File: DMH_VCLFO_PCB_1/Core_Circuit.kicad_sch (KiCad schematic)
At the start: 73 parts, among them Q1 BC548, Q2 BC558, Q3 BC548, Q4 BC548, Q5 BS170, Q6 J113, Q7 BC548, U10 TL074, U11 TL074, U12 TL074

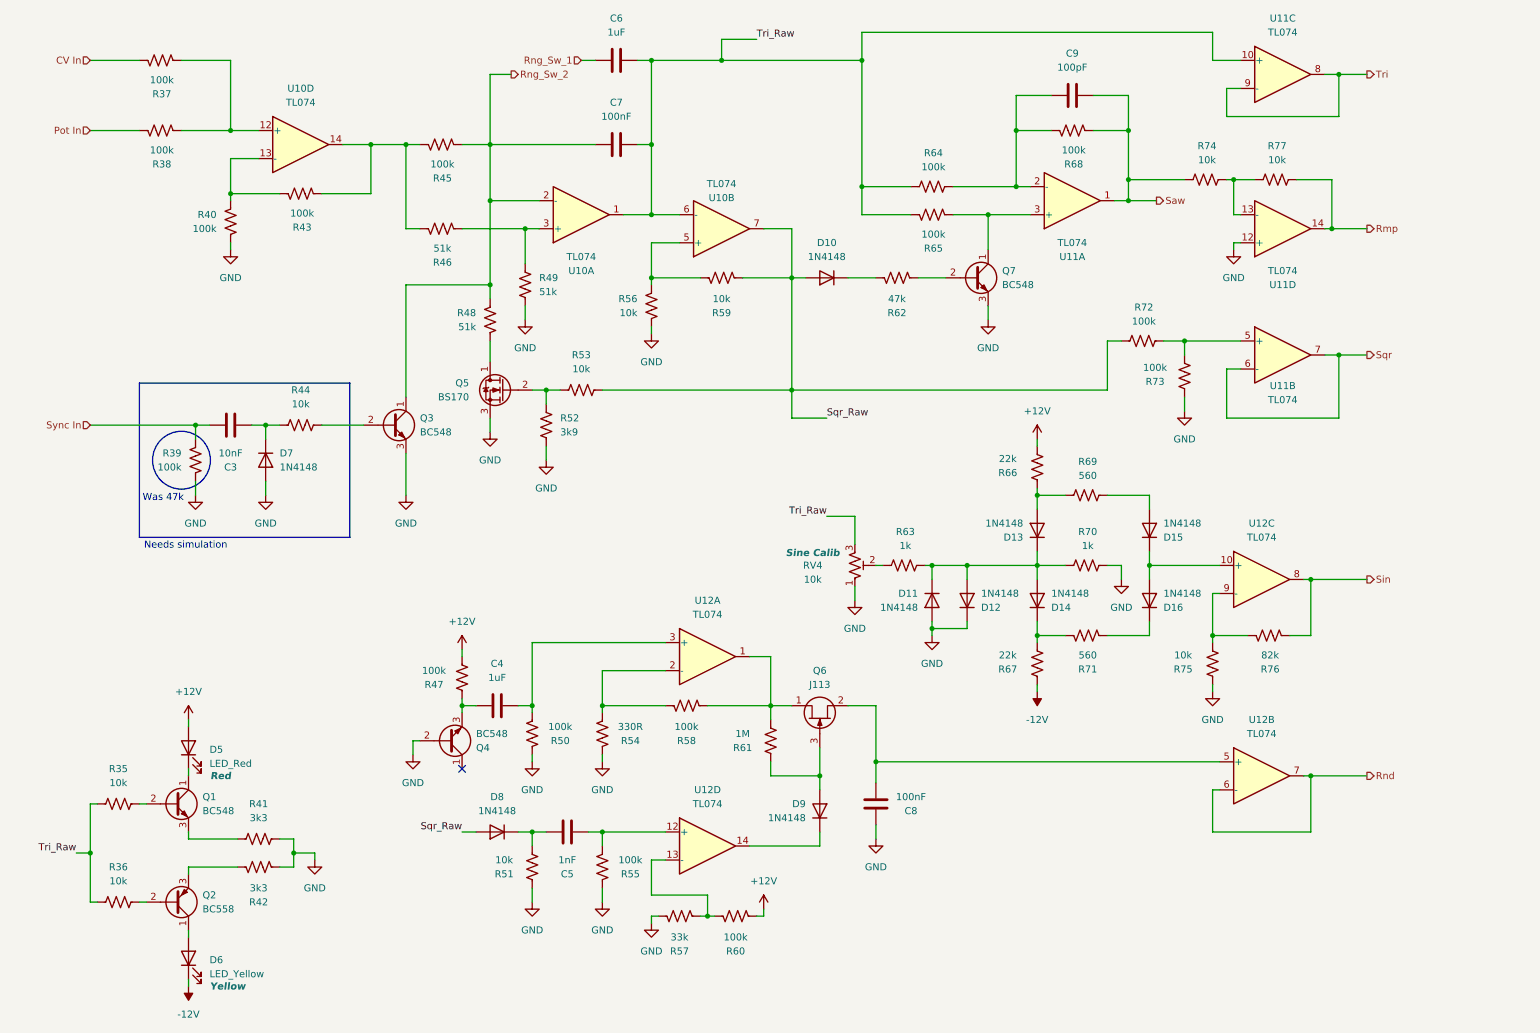
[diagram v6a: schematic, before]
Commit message: Improved sync input
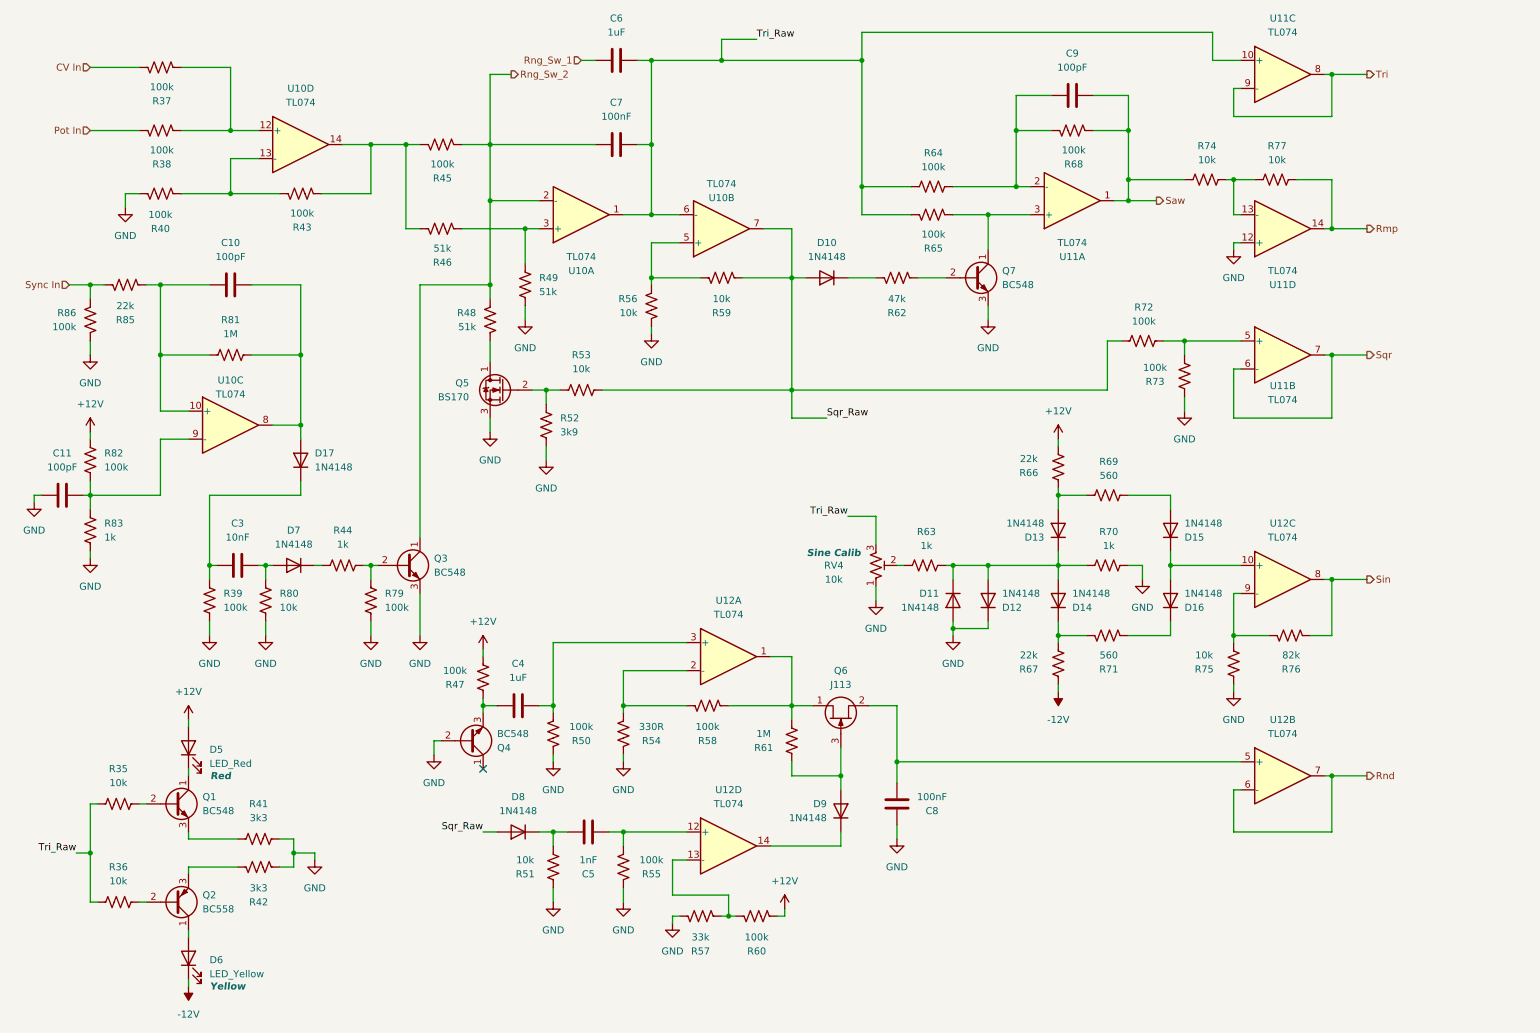
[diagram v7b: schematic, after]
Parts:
- added C10, C11: 100pF, Capacitor_THT:C_Disc_D4.3mm_W1.9mm_P5.00mm, symbol Device:C
- added D17: 1N4148, Diode_THT:D_DO-35_SOD27_P7.62mm_Horizontal, symbol Diode:1N4148
- added R79, R82, R86: 100k, Resistor_THT:R_Axial_DIN0207_L6.3mm_D2.5mm_P7.62mm_Horizontal, symbol Device:R_US
- added R80: 10k, Resistor_THT:R_Axial_DIN0207_L6.3mm_D2.5mm_P7.62mm_Horizontal, symbol Device:R_US
- added R81: 1M, Resistor_THT:R_Axial_DIN0207_L6.3mm_D2.5mm_P7.62mm_Horizontal, symbol Device:R_US
- added R83: 1k, Resistor_THT:R_Axial_DIN0207_L6.3mm_D2.5mm_P7.62mm_Horizontal, symbol Device:R_US
- added R85: 22k, Resistor_THT:R_Axial_DIN0207_L6.3mm_D2.5mm_P7.62mm_Horizontal, symbol Device:R_US
- added unit 3 of U10
- R44: value 10k -> 1k
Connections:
- net +12V: now also R82.1
- net GND: now also R40.1, C11.1, R79.2, R80.2, R83.2, R86.1; no longer D7.2 (A), R40.2
- net Sync In: now also R85.1, R86.2; no longer C3.1, R39.1
- net at R43.1, U10.13 (-): now also R40.2; no longer R40.1
- net at D7.1 (K), R44.1: no longer C3.2
- net at Q3.2 (B), R44.2: now also R79.1
- new net: C3.1, D17.1 (K), R39.1
- new net: C10.1, R81.1, R85.2, U10.10 (+)
- new net: C11.2, R82.2, R83.1, U10.9 (-)
- new net: C3.2, D7.2 (A), R80.1
- new net: C10.2, D17.2 (A), R81.2, U10.8
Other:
- note removed: "Needs simulation"
- note removed: "Was 47k"
- moved on the sheet: C3, C4, C5, C8, D11, D12, D13, D14, D15, D16, D7, D8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

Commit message: Annotations during breabboarding troubleshooting
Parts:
- D10, Q3: now not fitted
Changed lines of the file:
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@@
 		(stroke
 			(width 0)
-			(type default)
+			(type dash)
 		)
 	)
@@
 		(stroke
 			(width 0)
-			(type default)
+			(type dash)
 		)
 	)
@@
 	(wire
 		(pts
-			(xy 158.75 87.63) (xy 152.4 87.63)
+			(xy 158.75 95.25) (xy 152.4 95.25)
 		)
 		(stroke
 			(width 0)
-			(type default)
+			(type dash)
 		)
 	)
@@
 		(stroke
 			(width 0)
-			(type default)
+			(type dash)
 		)
 	)
@@
 		(stroke
 			(width 0)
-			(type default)
+			(type dash)
 		)
 	)
@@
 		(stroke
 			(width 0)
-			(type default)
+			(type dash)
 		)
 	)
@@
 		(stroke
 			(width 0)
-			(type default)
+			(type dash)
 		)
 	)
@@
 	(wire
 		(pts
-			(xy 152.4 87.63) (xy 152.4 82.55)
+			(xy 152.4 95.25) (xy 152.4 82.55)
 		)
 		(stroke
 			(width 0)
-			(type default)
+			(type dash)
 		)
 	)
@@
 		(stroke
 			(width 0)
-			(type default)
+			(type solid)
 		)
 	)
@@
 	(wire
 		(pts
-			(xy 96.52 162.56) (xy 99.06 162.56)
+			(xy 91.44 162.56) (xy 99.06 162.56)
 		)
 		(stroke
 			(width 0)
-			(type default)
+			(type dash)
 		)
 	)
@@
 	)
 	(label "Sqr_Raw"
-		(at 158.75 87.63 0)
+		(at 158.75 95.25 0)
 		(effects
 			(font
@@
 	)
 	(label "Sqr_Raw"
-		(at 96.52 162.56 180)
+		(at 91.44 162.56 180)
 		(effects
 			(font
@@
 		(in_bom yes)
 		(on_board yes)
-		(dnp no)
+		(dnp yes)
 		(fields_autoplaced yes)
 		(property "Reference" "Q3"
@@
 		(in_bom yes)
 		(on_board yes)
-		(dnp no)
+		(dnp yes)
 		(fields_autoplaced yes)
 		(property "Reference" "D10"
